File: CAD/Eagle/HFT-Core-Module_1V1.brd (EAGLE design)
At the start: 96.5 x 96.5 mm, 528 parts, among them Q0321 ABS07-32.768KHZ, Q1321 ABS07-32.768KHZ, Q2211 ABM3B-32.0000MHZ, Q2311 ABM3B-16.0000MHZ, T1051 MMBT2222, T1111 MMBT2222, T1121 MMBT2222, T1131 MMBT2222, U0111 STM32L4Z_144PIN_SMPS, U0521 PCAL6416APW, U0621 PCAL6416APW, U0711 IS25LP032D, U0721 IS25LP032D, U0801 CAT24C64, U0911 ZIO_EINK_1IN54, U1001 MIDAS_MCCOG21605B6W-FPTLWI, U1301 BNO085, U1401 BME680, U1501 LM4120IM5-3.0, U1511 MAX5217, U1531 CFPT-141-20MHZ, U1541 OPA354, U1542 LPV811, U1601 Si5338, U1651 TS5A23166, U1701 PCM1863, U1801 WM8523, U1901 SIM868, U2201 SX1262, U2271 PE4259, U2301 AX5243, U2401 LM53603-Q1, U2501 BQ24193, U2541 LPV811, U2601 BQ25570, U2681 TS5A23166, U2701 TPS62056, U2801 TPS62051, U2851 MCP4661-104E-MS, U2901 TS5A23166, U3001 TS5A23166, U3101 TS5A23166, U3201 TS5A23166, U3491 TS5A23166, U3492 TDK B4310, X1201 TTE_EN11-HSM, X1951 MICROSIM-8P_SDCARD-8P_MOLEX-1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, X2411 WIRE-TO-BOARD_5MM08_1X02, X2551 JST_S3B-XH-A, X2601 WIRE-TO-BOARD_5MM08_1X02, X3301 MOLEX 105017-0001, X3401 SMA_SMT_AMPHENOL-901-143, X3411 SAMTEC SMA-J-P-H-RA-TH1, X3471 SMA_SMT_AMPHENOL-901-143, SAM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, X3481 SMA_SMT_AMPHENOL-901-143, SAM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, X3491 SMA_SMT_AMPHENOL-901-143, SAM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, X3501 CUI SJ1-3535NS, X3511 CUI SJ1-3535NS, X3611 2X20/90_1MM27_HARWIN_M50-3202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, X3612 2X20/90_1MM27_HARWIN_M50-3202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, X3631 2X20/90_1MM27_HARWIN_M50-3202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, X3632 2X20/90_1MM27_HARWIN_M50-3202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

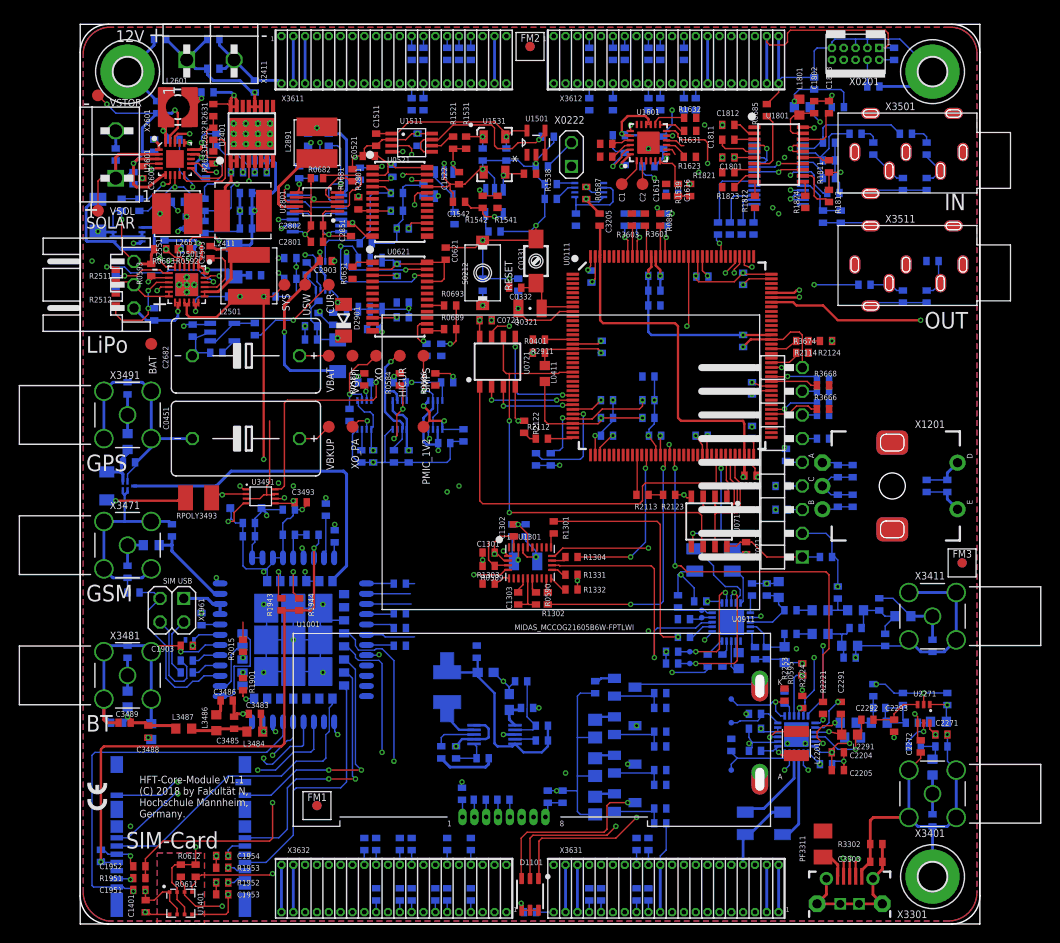
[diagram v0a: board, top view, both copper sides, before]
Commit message: HW_1V1 - CAD/Eagle - routing in the south east
Signed-off-by: Ulrich Habel <espero7757@gmx.net>
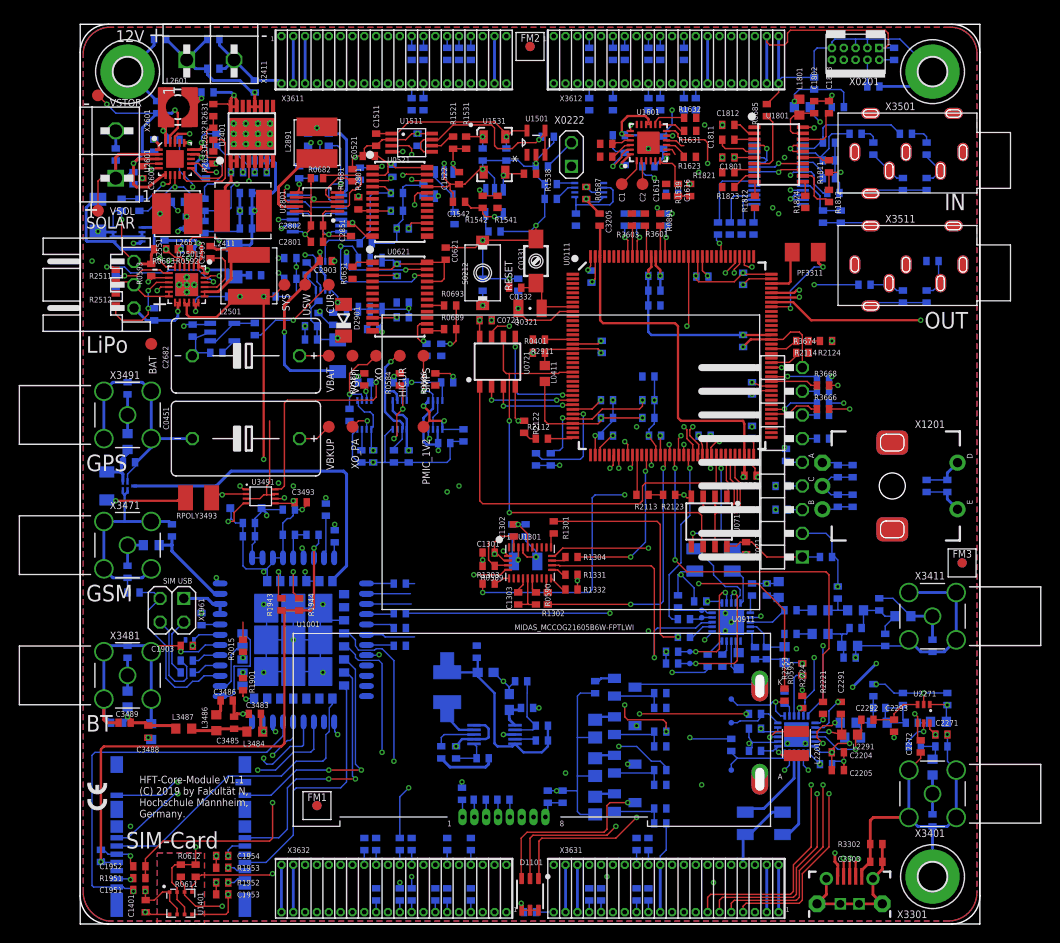
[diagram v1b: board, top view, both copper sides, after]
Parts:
- moved PF3311 63.5 mm to (77.8, 72.1), turned to 180 degrees
- moved C0404 0.32 mm to (67.0, 52.4)
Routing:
- net PE10: track 0.00 -> 82.9 mm, vias 0 -> 4
- net PE9: track 0.00 -> 82.7 mm, vias 0 -> 3
- net PE8: track 0.00 -> 82.3 mm, vias 0 -> 4
- net PA9: track 3.18 -> 84.6 mm, vias 0 -> 5
- net PS03: track 0.00 -> 71.5 mm, vias 0 -> 2
- net PS02: track 0.00 -> 68.2 mm, vias 0 -> 2
- net PS01: track 0.00 -> 66.1 mm, vias 0 -> 2
- net PS00: track 0.00 -> 65.6 mm, vias 0 -> 2
- net PF12: track 21.5 -> 61.2 mm, vias 2 -> 4
- net PA6: track 0.00 -> 39.0 mm, vias 0 -> 2
- net PG1: track 0.00 -> 38.4 mm, vias 0 -> 2
- net PG0: track 0.00 -> 37.8 mm, vias 0 -> 2
- net PA7: track 0.00 -> 37.6 mm, vias 0 -> 2
- net PB0: track 0.00 -> 35.3 mm, vias 0 -> 3
- net PC5: track 0.00 -> 33.6 mm, vias 0 -> 3
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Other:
- board text added: "HFT-Core-Module V1.1 (C) 2019 by Fakultät N, Hochschule Mannheim, Germany."
- board text removed: "HFT-Core-Module V1.1 (C) 2018 by Fakultät N, Hochschule Mannheim, Germany."

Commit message: HW_1V1 - CAD/Eagle - routing under the MCU
Signed-off-by: Ulrich Habel <espero7757@gmx.net>
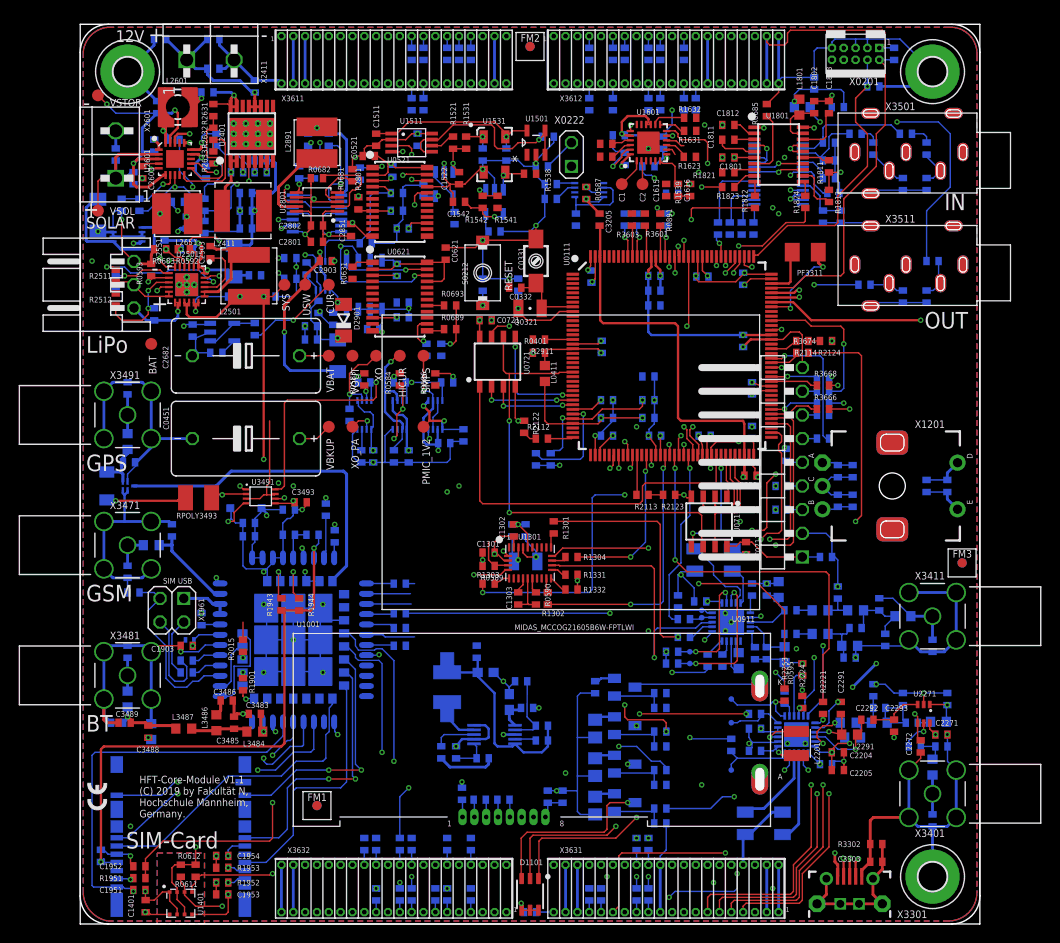
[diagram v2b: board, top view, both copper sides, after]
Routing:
- net PB13: track 0.00 -> 93.7 mm, vias 0 -> 4
- net EVT_S_OUT: track 0.00 -> 90.3 mm, vias 0 -> 3
- net PB15: track 0.00 -> 90.2 mm, vias 0 -> 3
- net PG9: track 0.00 -> 75.2 mm, vias 0 -> 2
- net PG12: track 0.00 -> 71.3 mm, vias 0 -> 2
- net PG10: track 0.00 -> 68.3 mm, vias 0 -> 2
- net PG11: track 0.00 -> 64.4 mm, vias 0 -> 2
- net PC6: track 0.00 -> 61.9 mm, vias 0 -> 4
- net AUDIO_DAC_LINEVOUTL: track 0.00 -> 37.3 mm, vias 0 -> 2
- net PD8: track 0.00 -> 33.7 mm, vias 0 -> 2
- net PA13: track 1.60 -> 35.0 mm
- net PE10: track 82.9 -> 115.1 mm, vias 4 -> 5
- net PE8: track 82.3 -> 111.5 mm, vias 4 -> 5
- net PD1: track 0.00 -> 28.6 mm, vias 0 -> 1
- net PD3: track 0.00 -> 28.2 mm, vias 0 -> 1
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
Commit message: HW_1V1 - CAD/Eagle - Today some routing in the south
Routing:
- net PD11: track 0.00 -> 123.6 mm, vias 0 -> 4
- net PD12: track 0.00 -> 123.1 mm, vias 0 -> 4
- net PG6: track 0.00 -> 113.3 mm, vias 0 -> 4
- net PC7: track 0.00 -> 111.6 mm, vias 0 -> 4
- net PG8: track 0.94 -> 106.9 mm, vias 0 -> 3
- net SIM_UART1_DTR: track 6.50 -> 112.2 mm, vias 0 -> 4
- net PD1: track 28.6 -> 99.6 mm, vias 1 -> 3
- net PF9: track 1.89 -> 68.2 mm, vias 0 -> 3
- net PC0: track 0.02 -> 65.4 mm, vias 1 -> 4
- net PD3: track 28.2 -> 93.1 mm, vias 1 -> 3
- net SIM_UART1_RTS: track 6.37 -> 43.2 mm, vias 0 -> 1
- net MCU_VBAT: track 3.67 -> 38.8 mm, vias 0 -> 1
- net SIM_UART1_RXD: track 6.23 -> 34.0 mm, vias 0 -> 2
- net EVT_S_OUT: track 90.3 -> 91.0 mm

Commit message: HW_1V1 - CAD/Eagle - Today some more routing in the mid-south
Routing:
- net MCU_VDD: track 33.9 -> 101.5 mm
- net PC13: track 0.00 -> 66.6 mm, vias 0 -> 2
- net PF8: track 0.00 -> 61.6 mm, vias 0 -> 2
- net PE6: track 0.00 -> 55.6 mm, vias 0 -> 3
- net MCU_VBAT: track 38.8 -> 92.0 mm, vias 1 -> 3

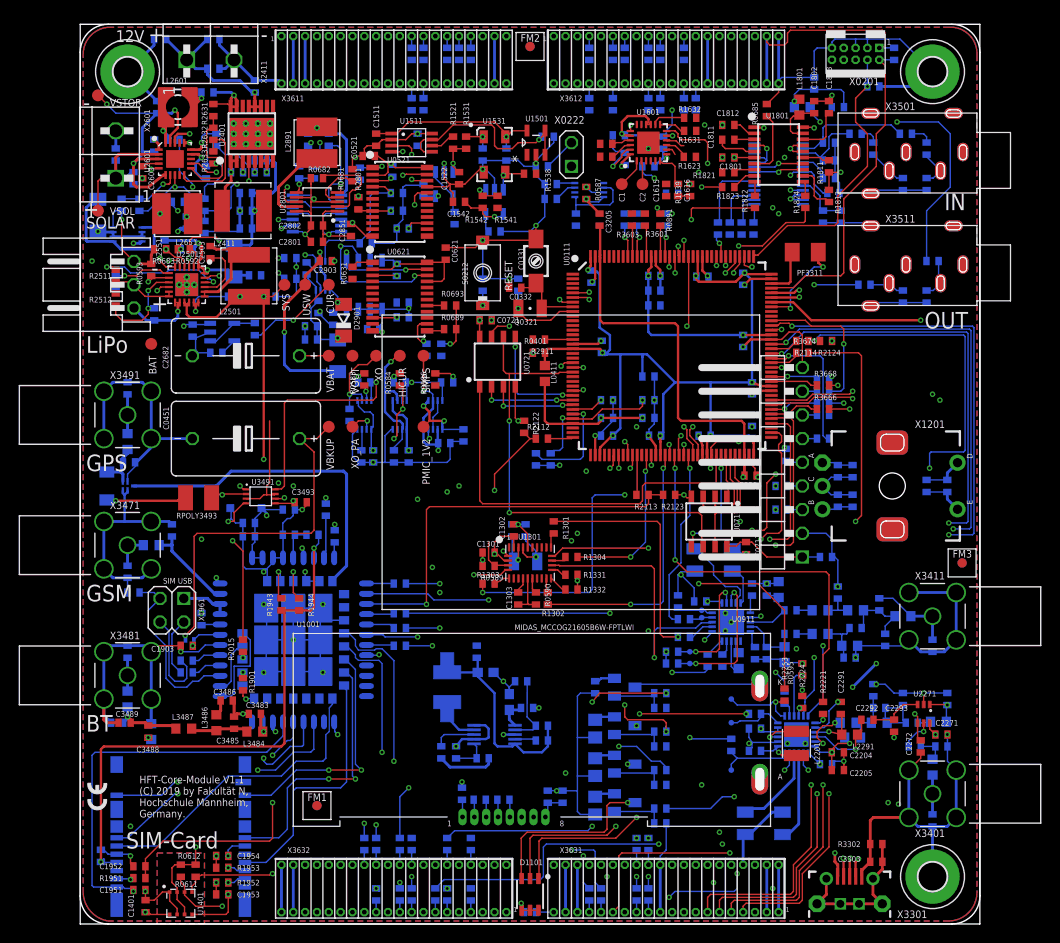
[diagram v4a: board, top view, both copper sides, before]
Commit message: HW_1V1 - CAD/Eagle - Routing around the MCU
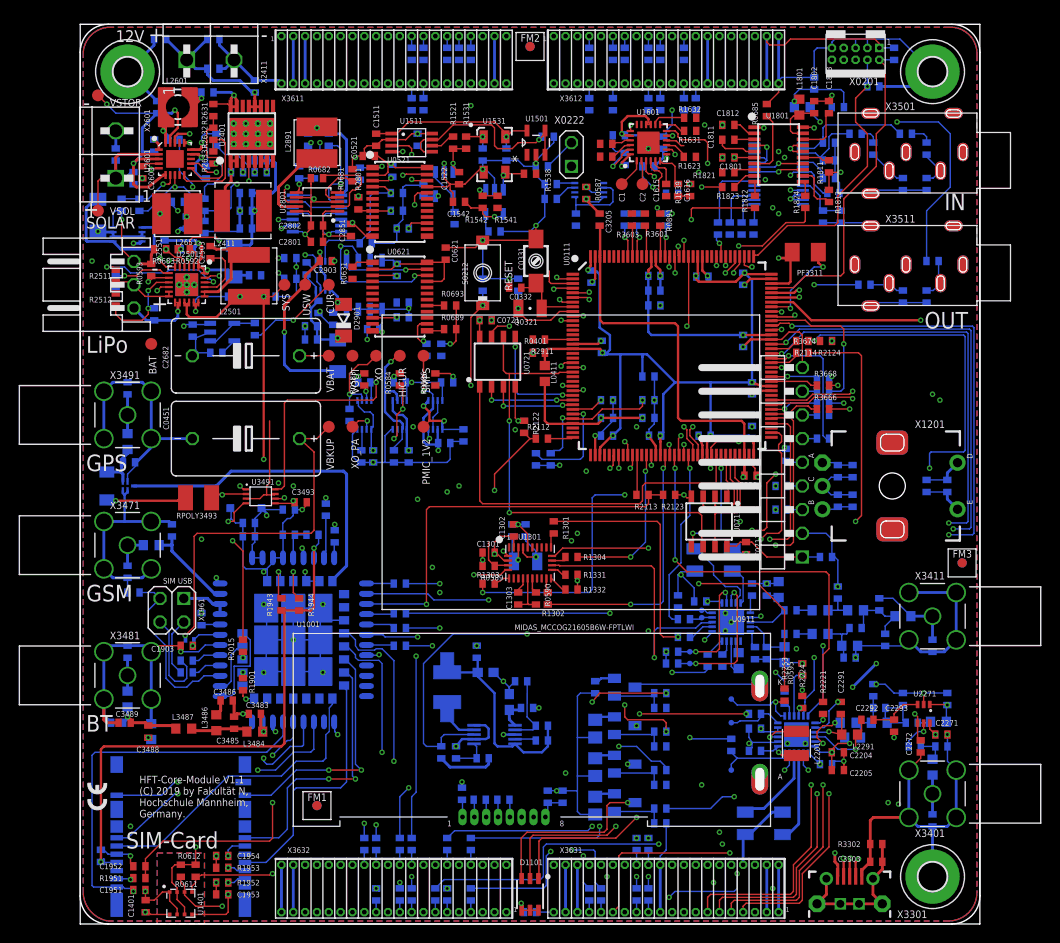
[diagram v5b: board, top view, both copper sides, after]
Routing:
- net MCU_NRST: track 1.59 -> 84.9 mm, vias 1 -> 4
- net PE3: track 0.00 -> 76.8 mm, vias 0 -> 4
- net PF1: track 0.00 -> 73.1 mm, vias 0 -> 2
- net PF0: track 0.00 -> 72.6 mm, vias 0 -> 2
- net PE5: track 4.58 -> 67.9 mm, vias 0 -> 2
- net VDDUSB: track 9.43 -> 60.4 mm, vias 1 -> 2
- net PC9: track 1.21 -> 34.8 mm, vias 0 -> 3
- net PA8: track 0.00 -> 30.5 mm, vias 0 -> 3
- net AX_8MHZ: track 0.00 -> 4.19 mm
- net PE4: track 0.86 -> 4.80 mm
- net SI5338_IN5: track 0.00 -> 3.33 mm
- net +3V3: track 151.9 -> 150.0 mm, vias 22 -> 25
- net GND: track 844.9 -> 845.7 mm

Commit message: HW_1V1 - CAD/Eagle - MCU east complete
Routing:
- net PG4: track 3.33 -> 94.2 mm, vias 0 -> 5
- net PD11: track 123.6 -> 183.5 mm, vias 4 -> 6
- net PD12: track 123.1 -> 180.0 mm, vias 4 -> 7
- net PB15: track 90.2 -> 146.4 mm, vias 3 -> 6
- net PB13: track 93.7 -> 142.3 mm, vias 4 -> 7
- net PC10: track 27.0 -> 27.6 mm
